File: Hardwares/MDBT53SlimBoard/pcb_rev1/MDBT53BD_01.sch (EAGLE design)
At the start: 48 parts, among them CN1 USB4105-GF-A, CN2 IF_6PIN, CN3 51296-0894, Q1 BSS84AKQBZ, SW1 SKRPACE010, SW2 SKTADAE010, U1 MDBT53, U2 XC6206P302MR-G, U3 RV-3028-C7, X1 FC-135_32.7680KA-AC

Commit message: 回路図の修正
・RTCC、TFT回路を削除
（変換基板で代用させるための措置）
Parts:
- removed C11: UMK105B7104KV-FR, Parts:CAP_0402N
- removed C12: UMK105B7104KV-FR, Parts:CAP_0402K
- removed CN3: 51296-0894, Connectors:51296-0894
- removed Q1: BSS84AKQBZ, Parts:BSS84AKQBZ
- removed R10, R11, R14, R8, R9: CRCW040210K0JNEDC, Parts:RESISTOR_0402N
- removed R12: CRCW040220K0FKEDC, Parts:RESISTOR_0402N
- removed R13: CRCW04025K10FKEDC, Parts:RESISTOR_0402N
- removed SW1: SKRPACE010, Parts:SKRPACE010
- removed SW2: SKTADAE010, Parts:SKTADAE010
- removed U1: MDBT53, Modules:MDBT53
- removed U3: RV-3028-C7, ICs:RV-3028-C7
- added CN4: IF_4PIN, Connectors:IF_4PIN
- added CN5: IF_6PIN, Connectors:IF_6PIN
- added MDBT1: MDBT53, MDBT53_210707:MDBT53
- added R15: CRCW04022R20FKEDC, Parts:RESISTOR_0402N
- added R16, R17: CRCW040227R0FKEDC, Parts:RESISTOR_0402N
- added SW3, SW4: SKRPACE010, Parts:SKRPACE010
- X1: value FC-135_32.7680KA-AC -> NX3215SA-32.768K-STD-MUA-9; device Parts:FC-135_32.7680KA-AC -> Parts:NX3215SA-32.768K-STD-MUA-9
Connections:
- removed net LEDA: CN3.1, Q1.D
- removed net N$14: Q1.G, R12.1, R13.2
- removed net N$2: R10.2, U3.EVI
- removed net N$3: R11.2, U3.VBACKUP
- removed net USER_SW: SW1.P, SW1.P1, U1.P0.23
- new net MAIN_SW: MDBT1.P0.23, SW3.P, SW3.P1
- new net N$13: C6.1, FB2.2, R15.1
- new net N$16: CN1.D_N1, CN1.D_N2, D5.I/O_1, R17.1
- new net N$18: CN1.D_P1, CN1.D_P2, D5.I/O_2, R16.1
- new net SUB_SW: MDBT1.P0.24, SW4.P, SW4.P1
- net 0V: now also CN4.1, MDBT1.GND@1, MDBT1.GND@24, MDBT1.GND@42, MDBT1.GND@61, SW3.S, SW3.S1, SW4.S, SW4.S1; no longer C11.2, C12.2, CN3.2, R10.1, R11.1, SW1.S, SW1.S1, SW2.P, SW2.P1, U1.GND@1, U1.GND@24, U1.GND@42, U1.GND@61, U3.VSS
- net D_N: now also MDBT1.D-, R17.2; no longer CN1.D_N1, CN1.D_N2, D5.I/O_1, U1.D-
- net D_P: now also MDBT1.D+, R16.2; no longer CN1.D_P1, CN1.D_P2, D5.I/O_2, U1.D+
- net LED1: now also MDBT1.P0.28/AIN7; no longer U1.P0.28/AIN7
- net LED2: now also MDBT1.P0.29; no longer U1.P0.29
- net LED3: now also MDBT1.P0.30; no longer U1.P0.30
- net LED4: now also MDBT1.P0.31; no longer U1.P0.31
- net LED_CTRL: now also CN5.1, MDBT1.P1.09; no longer R13.1, U1.P1.09
- net N$15: now also MDBT1.VDDH; no longer U1.VDDH
- net RESET: now also MDBT1.RESET; no longer C12.1, R14.2, SW2.S, SW2.S1, U1.RESET
- net SWDCLK: now also MDBT1.SWDCLK; no longer U1.SWDCLK
- net SWDIO: now also MDBT1.SWDIO; no longer U1.SWDIO
- net TFT_CLK: now also CN5.6, MDBT1.P1.15; no longer CN3.6, U1.P1.15
- net TFT_CS: now also CN5.4, MDBT1.P1.12; no longer CN3.8, U1.P1.12
- net TFT_D_C: now also CN5.2, MDBT1.P1.11; no longer CN3.4, U1.P1.11
- net TFT_MOSI: now also CN5.5, MDBT1.P1.13; no longer CN3.5, U1.P1.13
- net TFT_RESET: now also CN5.3, MDBT1.P1.10; no longer CN3.3, U1.P1.10
- net TWI_SCL: now also CN4.3, MDBT1.P1.03/TWI; no longer R9.1, U1.P1.03/TWI, U3.SCL@
- net TWI_SDA: now also CN4.2, MDBT1.P1.02/TWI; no longer R8.1, U1.P1.02/TWI, U3.SDA@
- net TXD: now also MDBT1.P0.20; no longer U1.P0.20
- net VBUS_NRF: now also MDBT1.VBUS, R15.2; no longer C6.1, FB2.2, U1.VBUS
- net VDD_NRF: now also CN4.4, MDBT1.VDD; no longer C11.1, CN3.7, Q1.S, R12.2, R14.1, R8.2, R9.2, U1.VDD, U3.VDD
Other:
- note added: "RTCC回路接続用 汎用I/O接続ポート"
- note added: "TFTモジュール接続用 汎用I/O接続ポート"
- note added: "ピン対応 GND --> 1 SDA --> 2 SCL --> 3 VDD --> 4"
- note added: "ピン対応 P1.09 --> 1 P1.10 --> 2 P1.11 --> 3 P1.12 --> 4 P1.13 --> 5 P1.15 --> 6"
- note added: "変換基板インターフェース部"
- note removed: "TFTインターフェース部"
- note removed: "TFTモジュール接続用FPCコネクター"
- note removed: "バックライト制御回路"
- note removed: "リセットボタン"
- note removed: "時刻同期部"

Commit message: 回路図の修正
・２／３ページを入れ替え
・部品番号を入れ替え
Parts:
- removed CN5: IF_6PIN, Connectors:IF_6PIN
- removed R15: CRCW04022R20FKEDC, Parts:RESISTOR_0402N
- removed R16, R17: CRCW040227R0FKEDC, Parts:RESISTOR_0402N
- removed SW3, SW4: SKRPACE010, Parts:SKRPACE010
- added CN3: IF_6PIN, Connectors:IF_6PIN
- added R8, R9: CRCW040227R0FKEDC, Parts:RESISTOR_0402N
- added SW1, SW2: SKRPACE010, Parts:SKRPACE010
- R1: value CRCW04020000Z0EDC -> CRCW04021K20FKEDC
- R2: value CRCW04025K10FKED -> CRCW04021K20FKEDC
- R3: value CRCW04025K10FKED -> CRCW04021K50FKEDC
- R4: value CRCW04021K20FKEDC -> CRCW0402390RFKEDC
- R5: value CRCW04021K20FKEDC -> CRCW04025K10FKED
- R6: value CRCW04021K50FKEDC -> CRCW04025K10FKED
- R7: value CRCW0402390RFKEDC -> CRCW04022R20FKEDC
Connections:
- removed net N$15: MDBT1.VDDH, R1.1
- net 0V: now also R5.2, R6.2, SW1.S, SW1.S1, SW2.S, SW2.S1; no longer R2.2, R3.2, SW3.S, SW3.S1, SW4.S, SW4.S1
- net D_N: now also R9.2; no longer R17.2
- net D_P: now also R8.2; no longer R16.2
- net LED1: now also R1.1; no longer R4.1
- net LED2: now also R2.1; no longer R5.1
- net LED3: now also R3.1; no longer R6.1
- net LED4: now also R4.1; no longer R7.1
- net LED_CTRL: now also CN3.1; no longer CN5.1
- net MAIN_SW: now also SW1.P, SW1.P1; no longer SW3.P, SW3.P1
- net N$1: now also R1.2; no longer R4.2
- net N$10: now also R5.1; no longer R2.1
- net N$13: now also R7.1; no longer R15.1
- net N$16: now also R9.1; no longer R17.1
- net N$18: now also R8.1; no longer R16.1
- net N$4: now also R2.2; no longer R5.2
- net N$5: now also R3.2; no longer R6.2
- net N$6: now also R4.2; no longer R7.2
- net N$7: now also R6.1; no longer R3.1
- net SUB_SW: now also SW2.P, SW2.P1; no longer SW4.P, SW4.P1
- net TFT_CLK: now also CN3.6; no longer CN5.6
- net TFT_CS: now also CN3.4; no longer CN5.4
- net TFT_D_C: now also CN3.2; no longer CN5.2
- net TFT_MOSI: now also CN3.5; no longer CN5.5
- net TFT_RESET: now also CN3.3; no longer CN5.3
- net VBUS_NRF: now also R7.2; no longer R15.2
- net VDD_NRF: now also MDBT1.VDDH; no longer R1.2

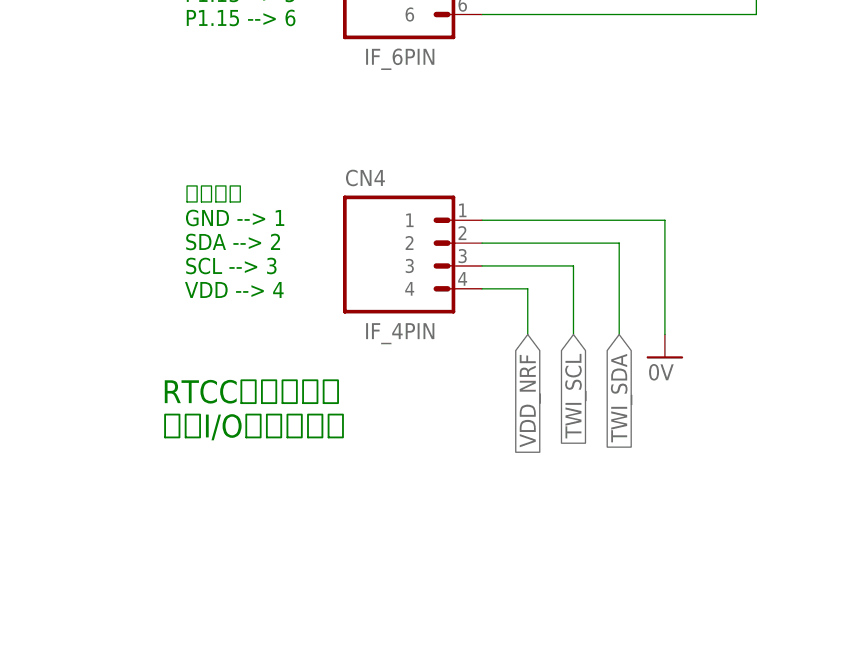
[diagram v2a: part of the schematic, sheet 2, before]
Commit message: 回路図の修正
・XL1／XL2が接続されていなかったため修正
・図面のレイアウトを小修正
・一部の部品名を変更
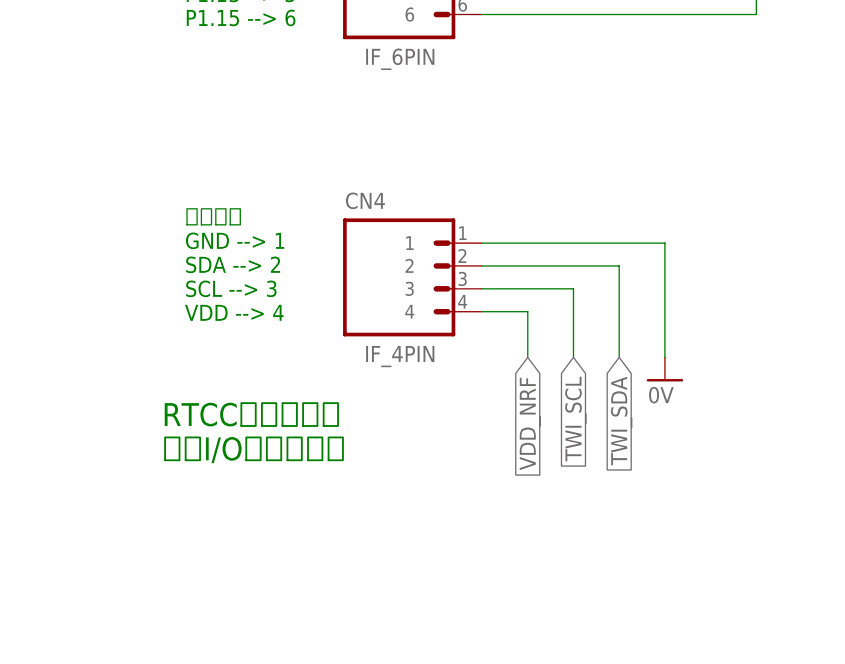
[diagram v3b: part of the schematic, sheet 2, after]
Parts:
- renumbered MDBT1 to U1
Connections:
- net XL1: now also U1.P0.00/XL1
- net XL2: now also U1.P0.01/XL2
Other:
- moved on the sheet: C3, C4, CN4

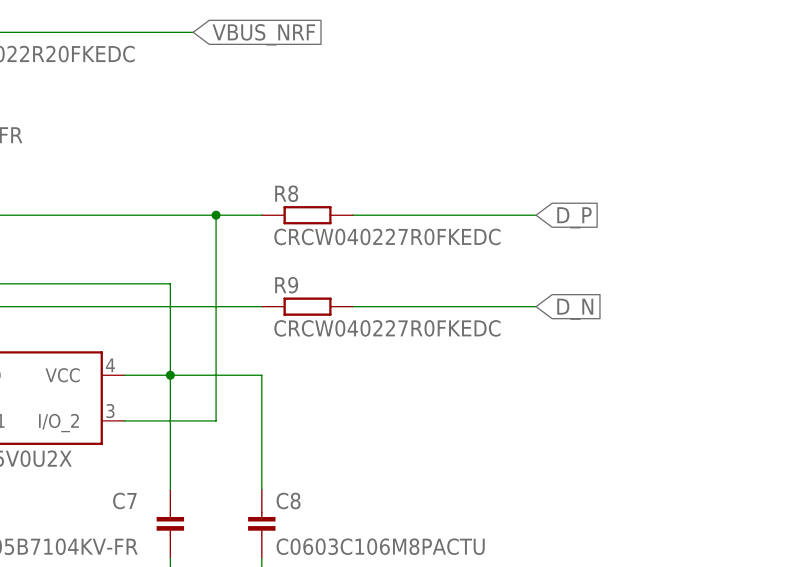
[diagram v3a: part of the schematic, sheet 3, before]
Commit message: 回路図の修正
・使用部品の変更
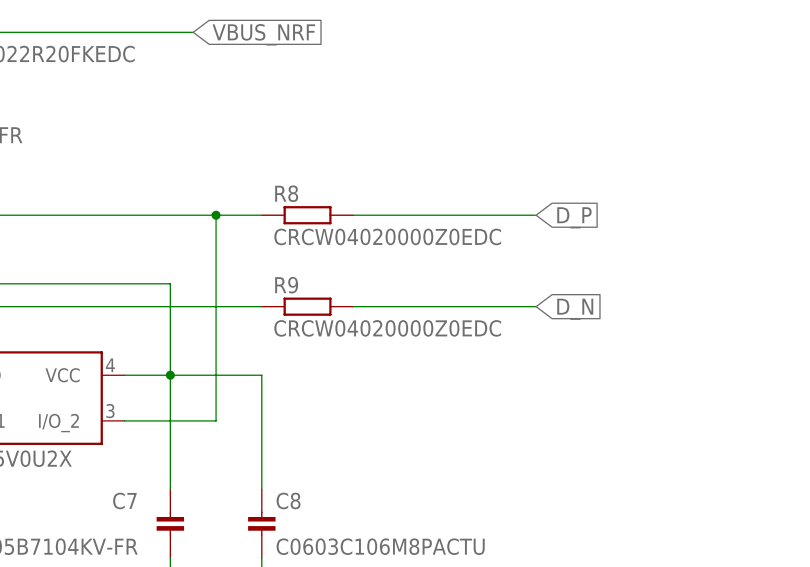
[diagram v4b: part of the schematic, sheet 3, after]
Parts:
- R8, R9: value CRCW040227R0FKEDC -> CRCW04020000Z0EDC
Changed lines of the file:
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@@
 <part name="X1" library="Parts" deviceset="NX3215SA" device="-32.768K-STD-MUA-9"/>
 <part name="R7" library="Parts" deviceset="RESISTOR" device="_0402N" value="CRCW04022R20FKEDC"/>
-<part name="R8" library="Parts" deviceset="RESISTOR" device="_0402N" value="CRCW040227R0FKEDC"/>
-<part name="R9" library="Parts" deviceset="RESISTOR" device="_0402N" value="CRCW040227R0FKEDC"/>
+<part name="R8" library="Parts" deviceset="RESISTOR" device="_0402N" value="CRCW04020000Z0EDC"/>
+<part name="R9" library="Parts" deviceset="RESISTOR" device="_0402N" value="CRCW04020000Z0EDC"/>
 <part name="SW1" library="Parts" deviceset="SKRPACE010" device=""/>
 <part name="GND14" library="Supply" deviceset="0V" device=""/>

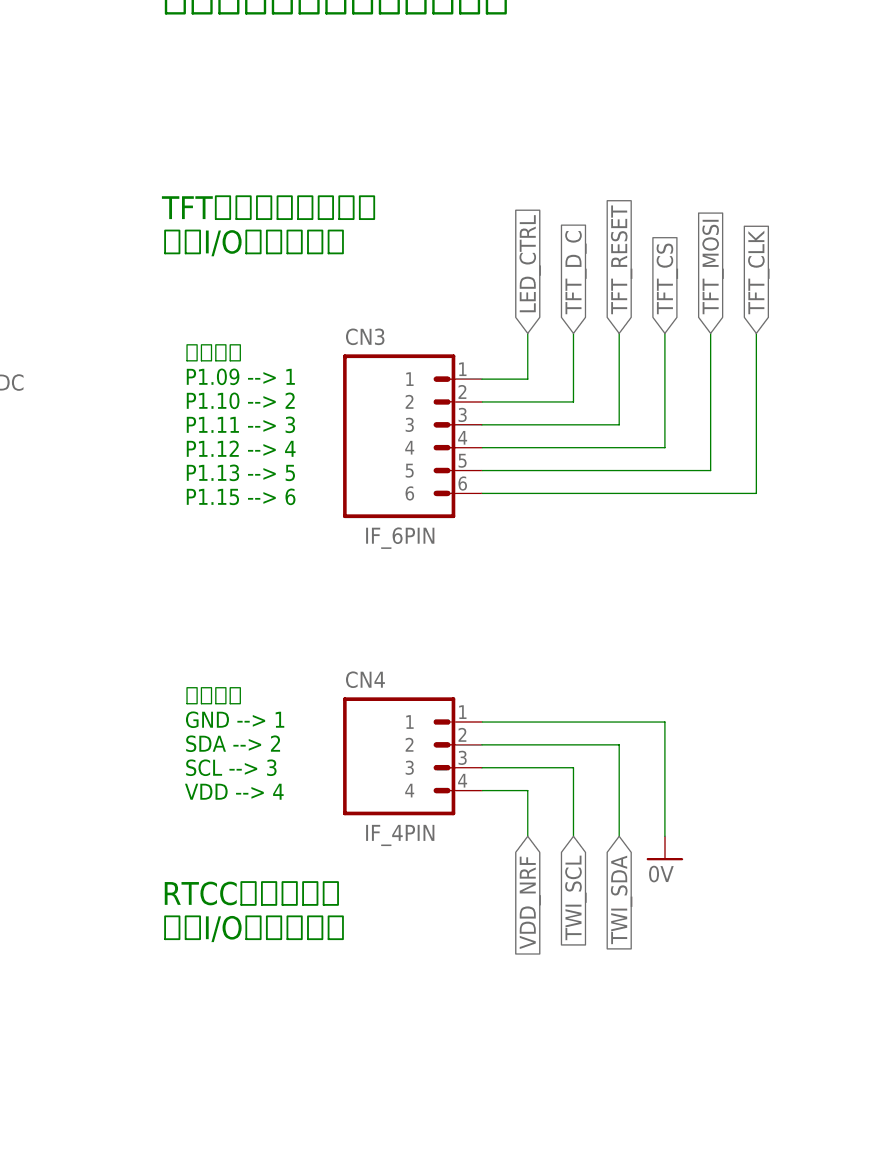
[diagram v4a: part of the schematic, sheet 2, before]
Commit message: 回路図を修正
・機能追加テスト用のGPIOを２点追加
・回路図の初版（PDF）を作成
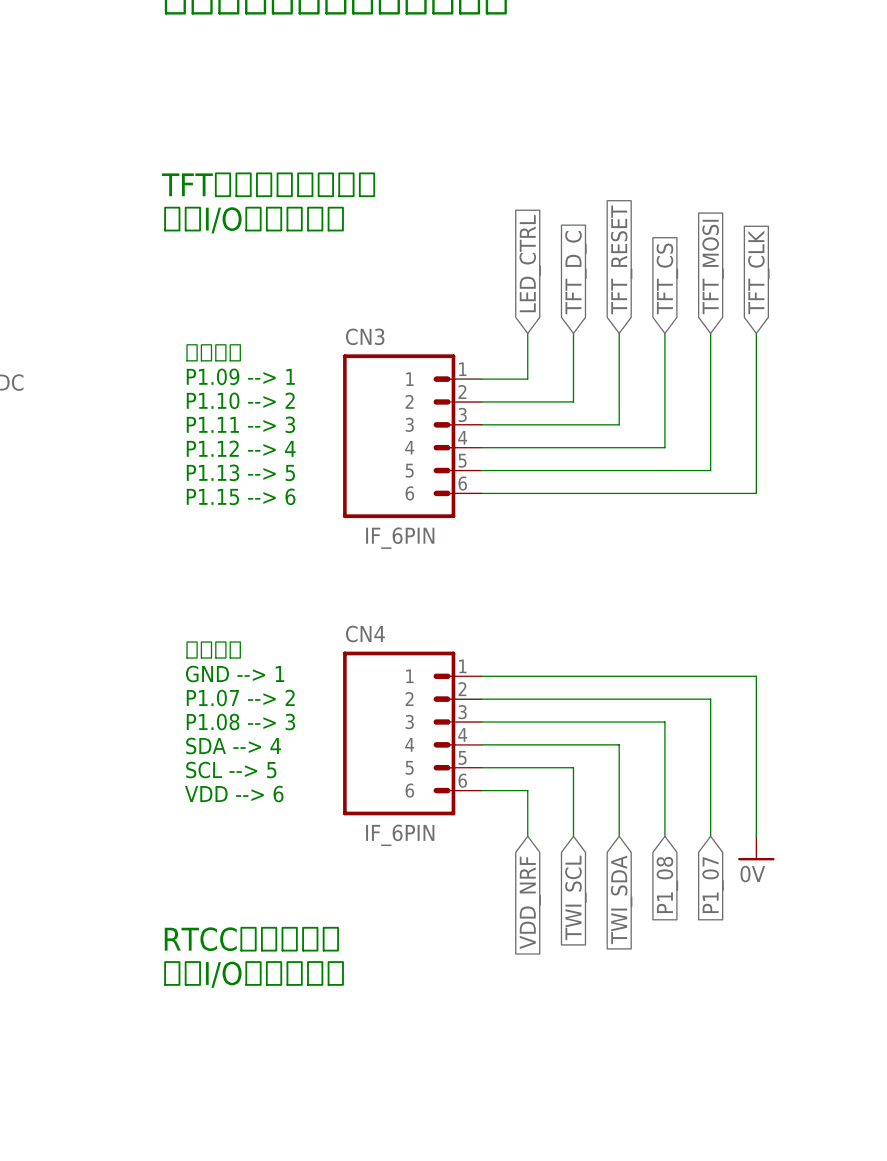
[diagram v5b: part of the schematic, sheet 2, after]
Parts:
- CN4: value IF_4PIN -> IF_6PIN; device Connectors:IF_4PIN -> Connectors:IF_6PIN
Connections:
- new net P1_07: CN4.2, U1.P1.07
- new net P1_08: CN4.3, U1.P1.08
- net TWI_SCL: now also CN4.5; no longer CN4.3
- net TWI_SDA: now also CN4.4; no longer CN4.2
- net VDD_NRF: now also CN4.6; no longer CN4.4
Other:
- note added: "ピン対応 GND --> 1 P1.07 --> 2 P1.08 --> 3 SDA --> 4 SCL --> 5 VDD --> 6"
- note removed: "ピン対応 GND --> 1 SDA --> 2 SCL --> 3 VDD --> 4"
